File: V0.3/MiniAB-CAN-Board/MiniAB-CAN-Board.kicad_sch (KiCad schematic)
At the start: 21 parts

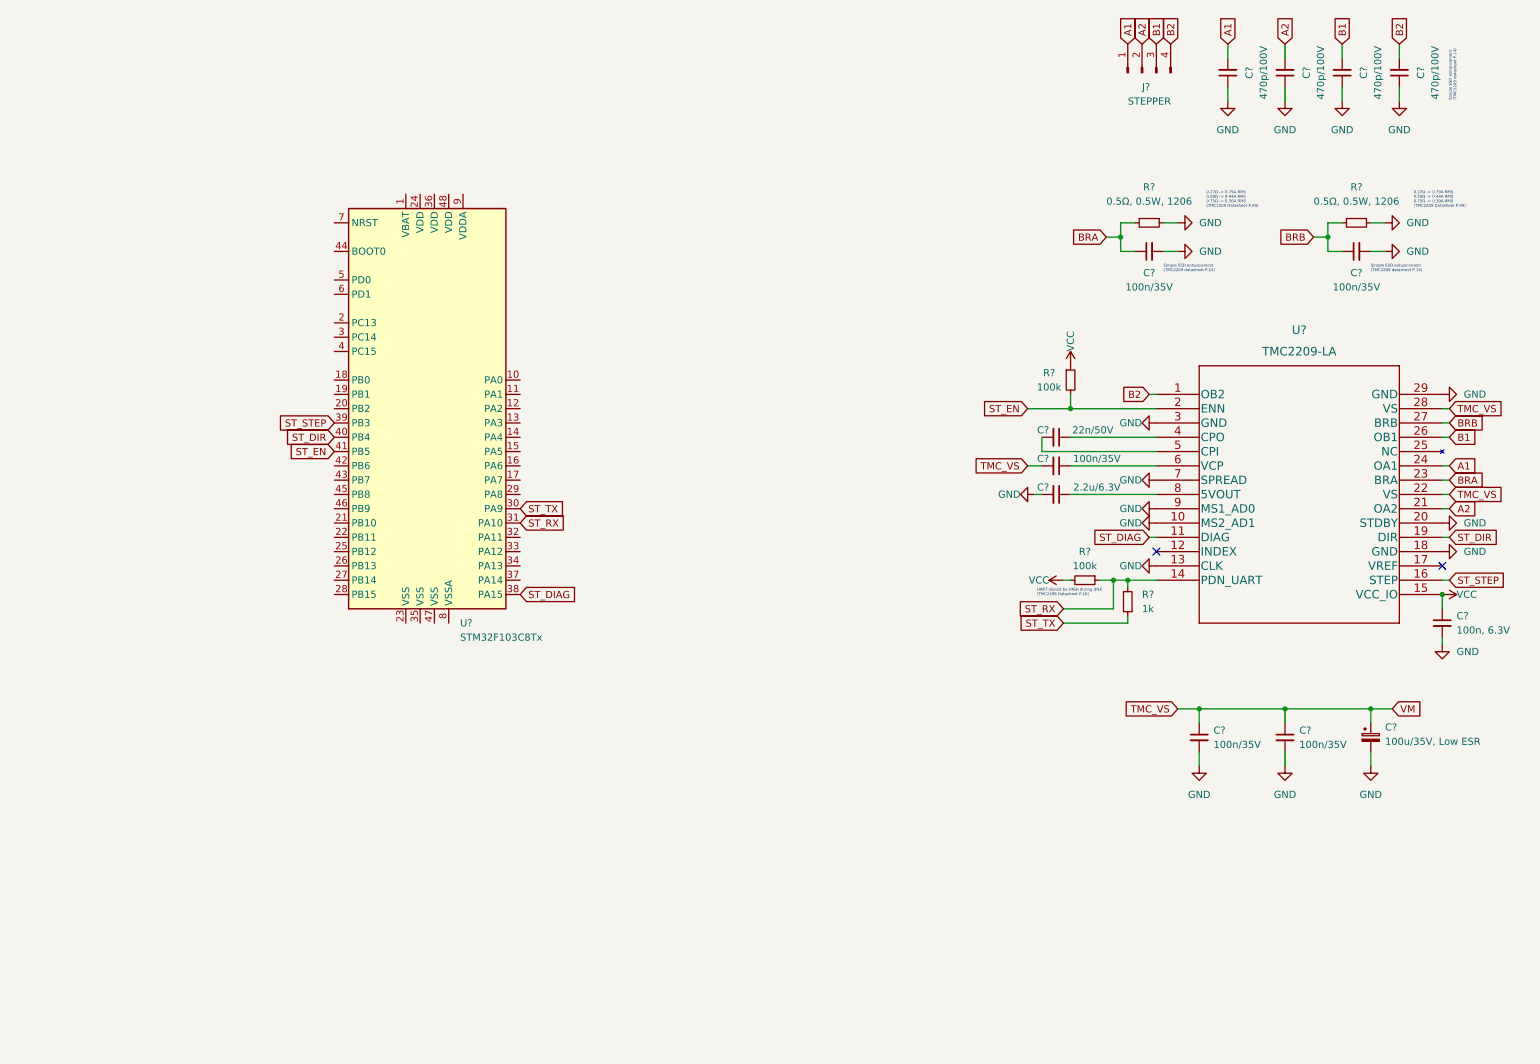
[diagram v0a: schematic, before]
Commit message: Add STM32 and ADXL to V0.3 Schematic
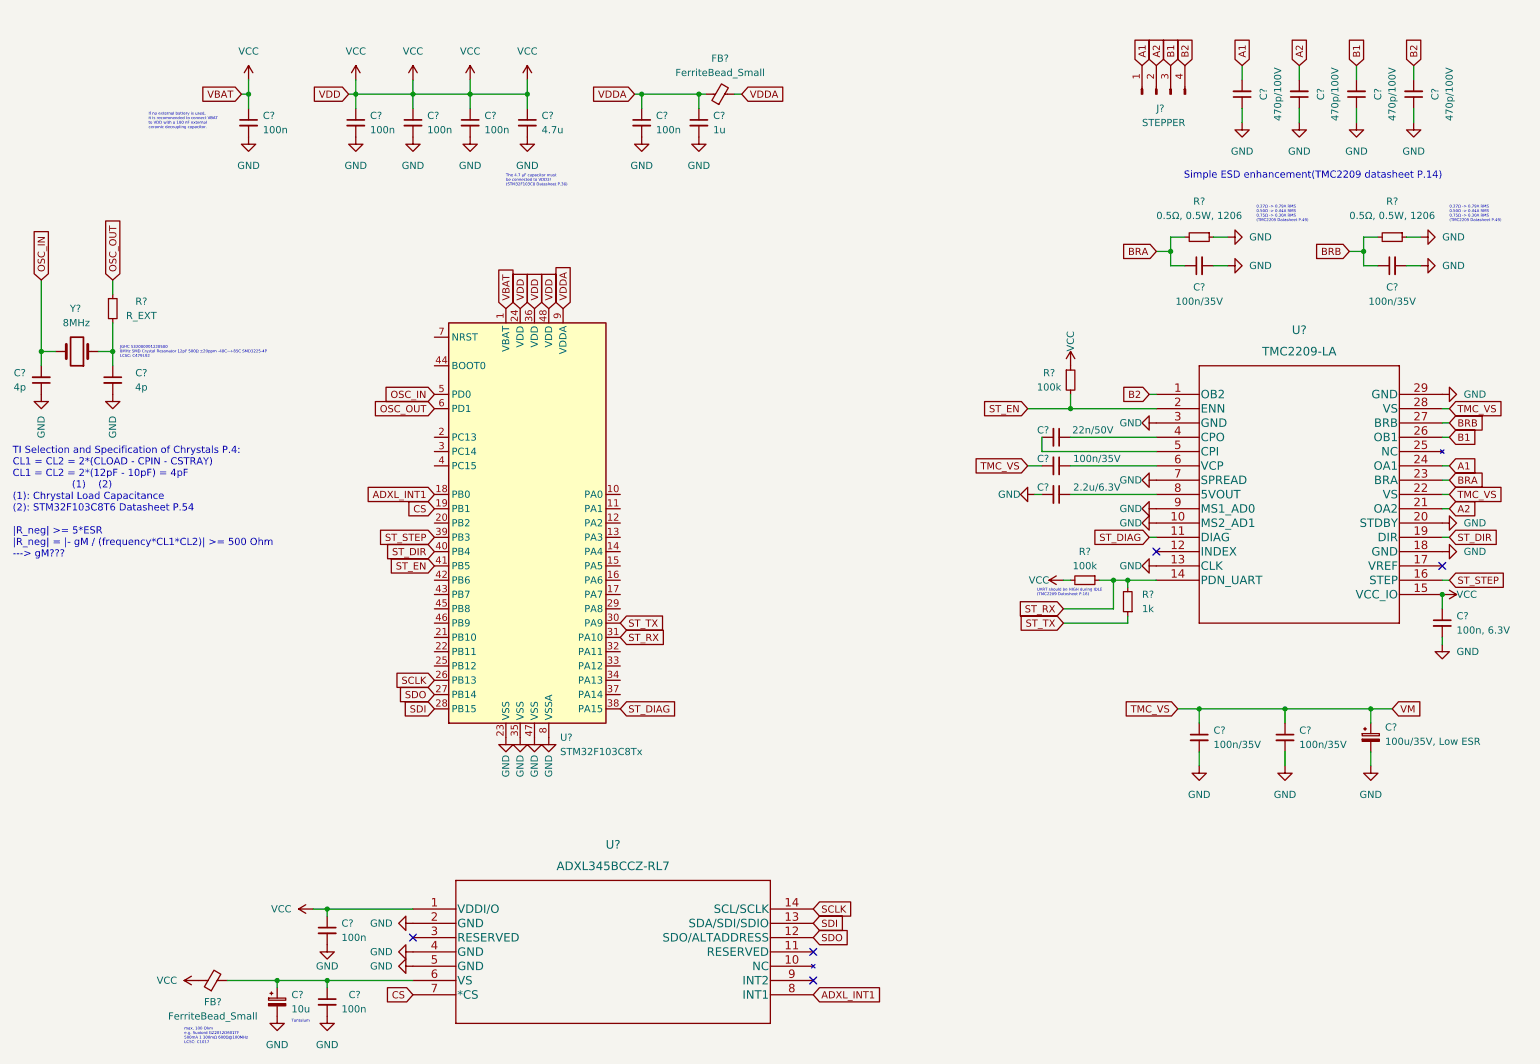
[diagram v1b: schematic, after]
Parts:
- added C? (x7): 100n, symbol Device:C_Small
- added C? (x2): 4p, symbol Device:C_Small
- added C?: 4.7u, symbol Device:C_Small
- added C?: 1u, symbol Device:C_Small
- added C?: 10u, symbol Device:C_Polarized_Small
- added FB? (x2): FerriteBead_Small, symbol Device:FerriteBead_Small
- added R?: R_EXT, symbol Device:R_Small
- added U?: ADXL345BCCZ-RL7, LGA_CC-14-1_ADI, symbol ADXL345BCCZ-RL7:ADXL345BCCZ-RL7
- added Y?: 8MHz, symbol Device:Crystal
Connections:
- net GND: now also U?.23 (VSS), U?.35 (VSS), U?.47 (VSS), U?.8 (VSSA), C?.1, C?.2, C?.2, C?.2, C?.2, C?.2, C?.2, C?.2, C?.2, C?.2, C?.2, C?.2, U?.2 (GND), U?.4 (GND), U?.5 (GND)
- net VCC: now also U?.1 (VBAT), U?.24 (VDD), U?.36 (VDD), U?.48 (VDD), C?.1, C?.1, C?.1, C?.1, C?.1, C?.1, FB?.1, U?.1 (VDDI/O)
- net ADXL_INT1: now reaches U?.18 (PB0)
- net ADXL_INT1: now also U?.8 (INT1)
- net CS: now reaches U?.19 (PB1)
- net CS: now also U?.7 (*CS)
- net SCLK: now reaches U?.26 (PB13)
- net SCLK: now also U?.14 (SCL/SCLK)
- net SDO: now reaches U?.27 (PB14)
- net SDO: now also U?.12 (SDO/ALTADDRESS)
- net SDI: now reaches U?.28 (PB15)
- net SDI: now also U?.13 (SDA/SDI/SDIO)
- net OSC_IN: now reaches U?.5 (PD0)
- net OSC_IN: now also C?.2, Y?.2
- net OSC_OUT: now reaches U?.6 (PD1)
- net OSC_OUT: now also R?.1
- net VDDA: now reaches U?.9 (VDDA)
- net VDDA: now also C?.1, C?.1, FB?.1, FB?.2
- new net: C?.1, C?.1, FB?.2, U?.6 (VS)
- new net: C?.1, R?.2, Y?.1
- no-connect marks 2 -> 5
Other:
- note added: "If no external battery is used, it is recommended to connect VBAT to VDD with a 100 nF external ceramic decoupling capacitor."
- note added: "JGHC S32080001220500 8MHz SMD Crystal Resonator 12pF 500Ω ±20ppm -40C~+85C SMD3225-4P LCSC: C479192"
- note added: "Simple ESD enhancement(TMC2209 datasheet P.14)"
- note added: "TI Selection and Specification of Chrystals P.4: CL1 = CL2 = 2*(CLOAD - CPIN - CSTRAY) CL1 = CL2 = 2*(12pF - 10pF) = 4pF (1) (2) (1): Chrystal Load Capacitance (2): STM32F103C8T6 Datasheet P.54 |R_neg| >= 5*ESR |R_neg| = |- gM / (frequency*CL1*CL2)| >= 500 Ohm ---> gM???"
- note added: "Tantalum"
- note added: "The 4.7 µF capacitor must be connected to VDD3! (STM32F103C8 Datasheet P.36)"
- note added: "max. 100 Ohm e.g. Sunlord GZ2012D601TF 500mA 1 300mΩ 600Ω@100MHz LCSC: C1017"
- note removed: "Simple ESD enhancement (TMC2209 datasheet P.14)"
- moved on the sheet: C?, J?, R?, U?
